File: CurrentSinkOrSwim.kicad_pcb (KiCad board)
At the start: 2 copper layers, 41.7 x 55 mm, 23 parts, among them P101 CONN_01X02, P102 CONN_01X03, P103 CONN_01X02, P301 CONN_01X01, Q301 BUK9575, U201 LMV358, U401 LM2931D-R

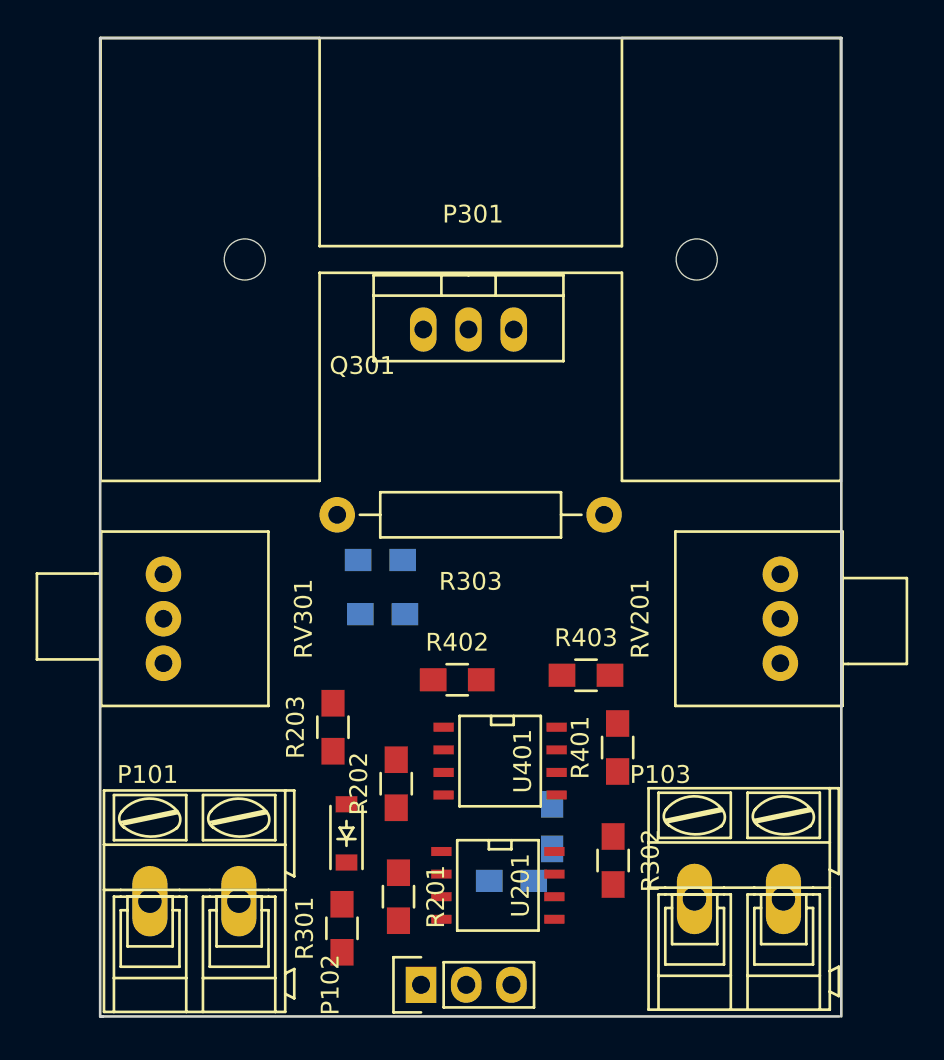
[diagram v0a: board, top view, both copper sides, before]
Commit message: This is the version of the file that has been submitted to OSH park
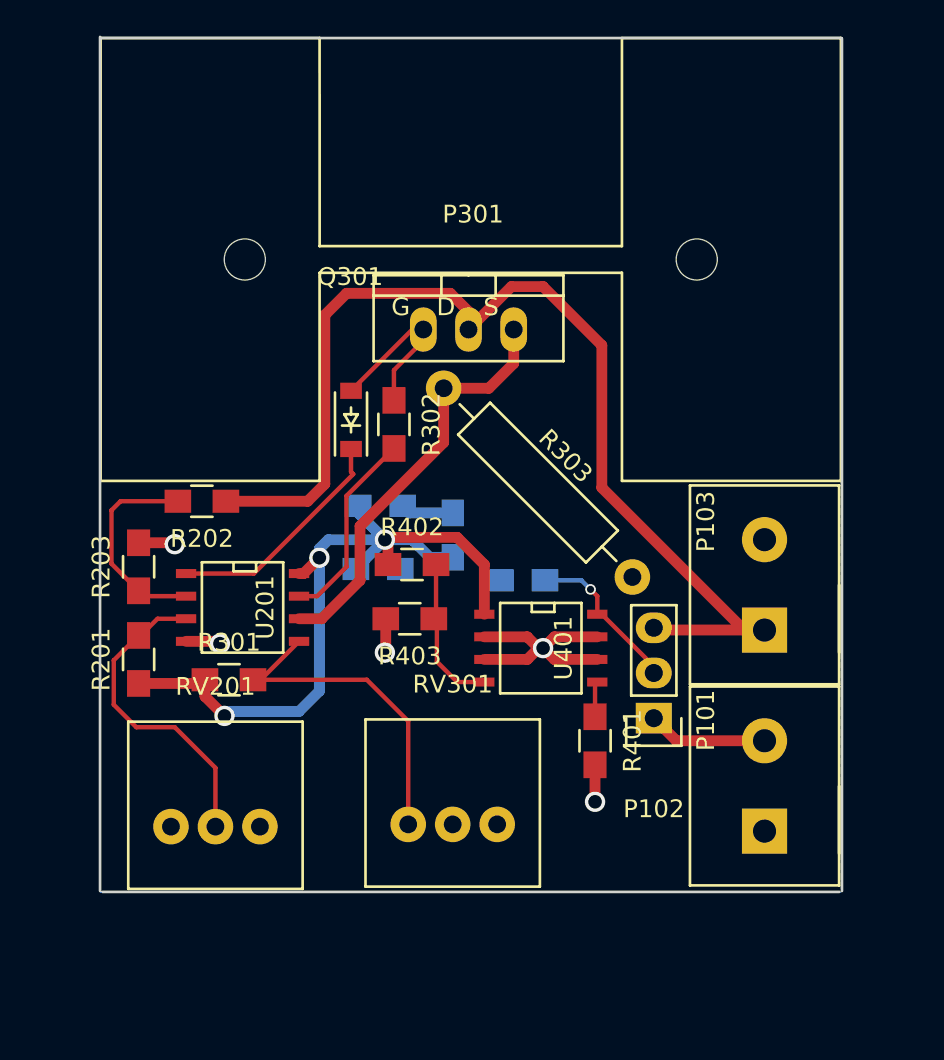
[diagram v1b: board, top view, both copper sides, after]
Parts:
- C201, C401, C402: value C -> .1
- D201: value D -> 1N4148
- P101, P103: footprint Connect:AK300-2 -> current:Terminal_Block_200_mil
- P301: value CONN_01X01 -> HEATSINK
- Q301: footprint TO_SOT_Packages_THT:TO-220_Neutral123_Vertical -> current:TO-220_GDS_Vertical
- R201: value R -> 28.7K
- R301: value R -> 68k
- RV201, RV301: value POT -> 10K
- U401: value LM2931D-R -> LM2931
- moved P101 35.1 mm to (101.3, 93.6), turned to 90 degrees
- moved RV201 33.8 mm to (70.5, 95.9), turned to 0 degrees
- moved R302 27.4 mm to (80.5, 73.3)
- moved D201 23.2 mm to (78.1, 73.0)
- moved U201 21.2 mm to (72.0, 83.6)
- moved RV301 19.9 mm to (83.8, 95.8), turned to 0 degrees
- moved P102 19.9 mm to (95.1, 89.8), turned to 180 degrees
- moved R201 19.8 mm to (66.2, 86.5), turned to 90 degrees
- moved R202 19.3 mm to (69.7, 77.6), turned to 180 degrees
- moved P103 18.1 mm to (101.3, 82.3), turned to 90 degrees
- moved C402 17.3 mm to (83.8, 79.5)
- moved C401 16.9 mm to (87.8, 82.0), turned to 180 degrees
- moved R301 15.3 mm to (71.2, 87.6), turned to 0 degrees
- moved R203 14.2 mm to (66.2, 81.3)
- moved R303 11.5 mm to (83.3, 71.2), turned to 315 degrees
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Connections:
- Q301 pad 1: /Current Control/Current_Sink+ -> /Current Control/FET_Gate
- Q301 pad 2: /Current Control/FET_Gate -> /Current Control/Current_Sink+
- R201 pad 1: Net-(R201-Pad1) -> 2.7V
- R201 pad 2: GND -> Net-(R201-Pad2)
- R301 pad 1: Net-(R301-Pad1) -> 2.7V
- R301 pad 2: GND -> Net-(R301-Pad2)
- RV201 pad 2: 2.7V -> Net-(R201-Pad2)
- RV201 pad 3: Net-(R201-Pad1) -> GND
- RV301 pad 1: Net-(RV301-Pad1) -> Net-(R301-Pad2)
- RV301 pad 2: 2.7V -> Net-(RV301-Pad2)
- RV301 pad 3: Net-(R301-Pad1) -> GND
- U201 pad 3: Net-(R201-Pad1) -> Net-(R201-Pad2)
- U201 pad 5: Net-(R301-Pad1) -> Net-(R301-Pad2)
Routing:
- net /Current Control/Current_Sink+: track 0.00 -> 63.6 mm
- net 2.7V: track 0.00 -> 45.4 mm, vias 0 -> 3
- net GND: track 0.00 -> 24.8 mm, vias 0 -> 5
- net Net-(Q301-Pad3): track 0.00 -> 23.5 mm
- net Net-(R301-Pad2): track 0.00 -> 19.0 mm
- net Net-(R201-Pad2): track 0.00 -> 17.9 mm
- net Net-(D201-Pad1): track 0.00 -> 13.2 mm
- net Net-(R202-Pad2): track 0.00 -> 11.9 mm
- net Net-(R302-Pad2): track 0.00 -> 11.1 mm
- net /Current Control/FET_Gate: track 0.00 -> 10.2 mm
- net /Power Regulation/Vin: track 0.00 -> 9.09 mm, vias 0 -> 1
- net Net-(R402-Pad2): track 0.00 -> 8.62 mm
- net Net-(P101-Pad2): track 0.00 -> 6.75 mm
- net Net-(R401-Pad1): track 0.00 -> 2.00 mm
- added copper zone on B.Cu, net GND
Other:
- board size 41.7 x 55 mm -> 41.7 x 48.1 mm
- net class Power added: clearance 0.3048, trace_width 0.6096, via_dia 1.143, via_drill 0.762
